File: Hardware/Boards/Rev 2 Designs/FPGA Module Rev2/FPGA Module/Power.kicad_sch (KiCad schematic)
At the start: 159 parts, among them U10 L78L33_SOT89, U11 INA236, U13 INA700AYWFR, U15 INA700AYWFR, U17 INA700AYWFR, U19 INA700AYWFR, U24 MP8796, U25 MP8796, U9 LT7200S

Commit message: Updates to FPGA and IO Module, layout studies and reference designs
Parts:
- removed C146, C147, C148, C161, C162, C163: 22uF, Capacitor_SMD:C_0805_2012Metric, symbol Device:C_Small
- removed C149, C164: 100nF, Capacitor_SMD:C_0201_0603Metric, symbol Device:C_Small
- removed C150, C165: 220nF, Capacitor_SMD:C_0201_0603Metric, symbol Device:C_Small
- removed C151: 1.8nF, Capacitor_SMD:C_0201_0603Metric, symbol Device:C_Small
- removed C152, C153, C154, C157: 100uF, Capacitor_SMD:C_0805_2012Metric, symbol Device:C_Small
- removed C155, C156: 560uF, Capacitor_Tantalum_SMD:CP_EIA-7343-31_Kemet-D, symbol Device:C_Polarized_Small_US
- removed C158, C159, C167, C168: 4.7uF, Capacitor_SMD:C_0201_0603Metric, symbol Device:C_Small
- removed C160: 470nF, Capacitor_SMD:C_0201_0603Metric, symbol Device:C_Small
- removed D7: 0V85 PG, LED_SMD:LED_0603_1608Metric, symbol Device:LED
- removed L1, L4: 220nH, FPGA Module:IND_SRP6530A_BRN, symbol Device:L
- removed R133: 12K, Resistor_SMD:R_0201_0603Metric, symbol Device:R_US
- removed R134: 27K, Resistor_SMD:R_0201_0603Metric, symbol Device:R_US
- removed R135, R136, R149, R152, R153, R161: 0R, Resistor_SMD:R_0201_0603Metric, symbol Device:R_US
- removed R137, R156: 2.2R, Resistor_SMD:R_0603_1608Metric, symbol Device:R_US
- removed R138, R142, R57, R6, R7: 3.3K, Resistor_SMD:R_0201_0603Metric, symbol Device:R_US
- removed R143, R144: 10K, Resistor_SMD:R_0201_0603Metric, symbol Device:R_US
- removed R147, R167: 24K, Resistor_SMD:R_0201_0603Metric, symbol Device:R_US
- removed R148, R168: 81K, Resistor_SMD:R_0201_0603Metric, symbol Device:R_US
- removed U24, U25: MP8796, FPGA Module:TQFN-4x5_MP8796B_MNP, symbol FPGA Module:MP8796GVT
- added C? (x2): 4.7uF, Capacitor_SMD:C_0201_0603Metric, symbol Device:C_Small
- added C? (x10): 22uF, Capacitor_SMD:C_0805_2012Metric, symbol Device:C_Small
- added C? (x4): 100uF, Capacitor_SMD:C_0805_2012Metric, symbol Device:C_Small
- added C?: 300pF, Capacitor_SMD:C_0201_0603Metric, symbol Device:C_Small
- added C? (x2): 560uF, Capacitor_Tantalum_SMD:CP_EIA-7343-31_Kemet-D, symbol Device:C_Polarized_Small_US
- added C?: 100nF, Capacitor_SMD:C_0201_0603Metric, symbol Device:C_Small
- added C?: 100nF, Capacitor_SMD:C_0402_1005Metric, symbol Device:C_Small
- added C? (x2): 1uF, Capacitor_SMD:C_0402_1005Metric, symbol Device:C_Small
- added D?: 0V85 PG, LED_SMD:LED_0603_1608Metric, symbol Device:LED
- added L?: 100nH, FPGA Module:IND_SRP6530A_BRN, symbol Device:L
- added R?: 10K, Resistor_SMD:R_0201_0603Metric, symbol Device:R_US
- added R?: 14K, Resistor_SMD:R_0201_0603Metric, symbol Device:R_US
- added R?: 24.9K, Resistor_SMD:R_0201_0603Metric, symbol Device:R_US
- added R?: 2.2R, Resistor_SMD:R_0603_1608Metric, symbol Device:R_US
- added R?: 24K, Resistor_SMD:R_0201_0603Metric, symbol Device:R_US
- added R?: 3.3K, Resistor_SMD:R_0201_0603Metric, symbol Device:R_US
- added R?: 3.48k, Resistor_SMD:R_0201_0603Metric, symbol Device:R_US
- added U?: TDA38840AUMA1, FPGA Module:PG-IQFN-36-2, symbol FPGA Module:TDA38840AUMA1
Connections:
- net 0V85_EN: now also U?.27 (EN)
- net 0V85_PG: now also D?.2 (A), R?.1, U?.2 (PGOOD)
- net 0V85_SNS: now also C?.1, C?.1, C?.1, C?.1, C?.1, C?.1, C?.1, C?.1, L?.2, R?.2
- net 3V3_AON: now also R?.2
- net GND: now also C?.2, C?.2, C?.2, C?.2, C?.2, C?.2, C?.2, C?.2, C?.2, C?.2, C?.2, C?.2, C?.2, C?.2, C?.2, C?.2, C?.2, C?.2, C?.2, C?.2, C?.2, D?.1 (K), R?.1, R?.1, R?.1, R?.1, U?.31 (VSENM), U?.32 (AGND), U?.7 (PGND)
- net PP_VUSB: now also C?.1, C?.1, C?.1, C?.1, C?.1, C?.1, C?.1, C?.1, C?.1, C?.1, C?.1, C?.1, U?.20 (PVIN), U?.3 (VIN)
- new net: C?.1, C?.1, U?.4 (VCC/LDO), U?.5 (VDRV)
- new net: C?.2, R?.1, R?.2, U?.30 (FB)
- new net: R?.2, U?.36 (TON/MODE)
- new net: R?.2, U?.1 (ILIM)
- new net: C?.1, R?.1
- new net: R?.2, U?.26 (BOOT)
- new net: L?.1, U?.11 (SW)
- new net: C?.2, U?.25 (PHASE)
- new net: R?.2, U?.29 (SS/LATCH)
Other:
- moved on the sheet: C102, C110, C118, C140, C141, C142, C143, C144, C145, C166, C169, C170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

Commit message: FPGA Module Rev 2 Layout Begun
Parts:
- removed C172, C173: 47uF, Capacitor_SMD:C_0603_1608Metric, symbol Device:C_Small
- removed L7: 300nH, Inductor_SMD:L_Taiyo-Yuden_MD-3030, symbol Device:L
- removed R101: 3.3K, Resistor_SMD:R_0201_0603Metric, symbol Device:R_US
- removed R68, R73: 33R, Resistor_SMD:R_0201_0603Metric, symbol Device:R_US
- removed TP33, TP45: Test Point, FPGA Module:Test Point 0.5mm No Silk, symbol Connector:TestPoint
- removed U13: INA700AYWFR, FPGA Module:INA700_AYWFR, symbol FPGA Module:INA700
- added C95, C96: 22uF, Capacitor_SMD:C_0805_2012Metric, symbol Device:C_Small
- added C98: 100pF, Capacitor_SMD:C_0603_1608Metric, symbol Device:C_Small
- added L5: 1uH, Inductor_SMD:L_1210_3225Metric, symbol Device:L
- added M1: Fan_4pin, Connector:FanPinHeader_1x04_P2.54mm_Vertical, symbol Motor:Fan_4pin
- added R69: 33R, Resistor_SMD:R_0201_0603Metric, symbol Device:R_US
- added R75: 3.3K, Resistor_SMD:R_0201_0603Metric, symbol Device:R_US
- added TP26: Test Point, FPGA Module:Test Point 0.5mm No Silk, symbol Connector:TestPoint
- C94: value 100nF -> 22uF; footprint Capacitor_SMD:C_0201_0603Metric -> Capacitor_SMD:C_0805_2012Metric
- R57: renamed from R63; value 33K -> 43K
- R67: renamed from R141; value 8.06K -> 100K
- R70: value 3.3K -> 10K
- gave numbers to parts that had none: 33
- renumbered C175 to C100, C176 to C101, C177 to C102, C178 to C103, C180 to C104, C182 to C105, C184 to C106, C179 to C107, C181 to C108, C183 to C109, C185 to C110, C86 to C64, C73 to C65, C88 to C66, C89 to C67, C90 to C68, C118 to C69, C83 to C70, C84 to C71, C81 to C72, C82 to C73, C79 to C74, C80 to C75, C77 to C76, C78 to C77, C85 to C78, C144 to C79, C145 to C80, C140 to C81, C166 to C82, C169 to C83, C110 to C84, C92 to C85, C87 to C86, C141 to C87, C170 to C88, C171 to C89, C186 to C90, C142 to C92, C102 to C93, C143 to C97, C174 to C99, D8 to D10, D11 to D7, D10 to D8, L3 to L2, L5 to L3, L2 to L4, R56 to R35, R58 to R37, R61 to R39, R62 to R40, R96 to R45, R105 to R46, R106 to R47, R64 to R48, R65 to R49, R87 to R50, R91 to R51, R92 to R52, R66 to R53, R132 to R54, R146 to R55, R150 to R56, R139 to R58, R78 to R59, R94 to R60, R85 to R61, R76 to R62, R67 to R63, R140 to R64, R82 to R65, R83 to R66, R145 to R68, R151 to R71, R154 to R72, R155 to R73, R157 to R74, R98 to R76, R99 to R77, R100 to R78, R102 to R79, TP28 to TP22, TP47 to TP23, TP39 to TP24, TP36 to TP25, TP42 to TP27, TP43 to TP28, TP44 to TP29, TP46 to TP30, U15 to U11, U11 to U6, U19 to U7, U9 to U8, U17 to U9
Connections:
- net 0V9_ISNS_ALERT is gone; now on net GND: R70.1
- net +3V3: no longer C94.1, R70.2
- net GND: now also C95.2, C96.2, C98.2, M1.1 (-), R75.1
- net 0V85_FB: now reaches C63.2, R38.1, R41.2, U5.30 (FB)
- net 0V85_LX: now reaches L1.1, U5.11 (SW)
- net +0V9 renamed 5V0
- net 5V0: now also C94.1, C95.1, C96.1, L5.2, M1.2 (+)
- net 0V9_EN renamed 5V0_EN
- net 5V0_EN: now also R75.2, TP26.1
- net 0V9_FB renamed 5V0_FB
- net 0V9_LX renamed 5V0_LX
- net 5V0_LX: now also L5.1
- new net: C98.1, M1.4 (PWM), R69.1, R70.2
- new net FAN_PWM: R69.2
- no-connect marks 1 -> 4
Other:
- note added: "5V 1A"
- note removed: "0V9 3A"
- moved on the sheet: D6, L1, R36, R76, R77, R78, R79, TP27, TP28, TP29, TP30

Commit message: Completed B2B and HyperRam routing
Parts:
- M1: footprint Connector:FanPinHeader_1x04_P2.54mm_Vertical -> Connector_JST:JST_GH_SM04B-GHS-TB_1x04-1MP_P1.25mm_Horizontal
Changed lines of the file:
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@@
 			)
 		)
-		(property "Footprint" "Connector:FanPinHeader_1x04_P2.54mm_Vertical"
+		(property "Footprint" "Connector_JST:JST_GH_SM04B-GHS-TB_1x04-1MP_P1.25mm_Horizontal"
 			(at 360.68 315.976 0)
 			(effects

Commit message: Rev 2 PCB's and Heatsink PCB's complete
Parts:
- removed C78: 1uF, Capacitor_SMD:C_0402_1005Metric, symbol Device:C_Small
- C98: footprint Capacitor_SMD:C_0603_1608Metric -> Capacitor_SMD:C_0201_0603Metric
- M1: footprint Connector_JST:JST_GH_SM04B-GHS-TB_1x04-1MP_P1.25mm_Horizontal -> Connector_JST:JST_SH_BM04B-SRSS-TB_1x04-1MP_P1.00mm_Vertical
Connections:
- net +0V85: now also C62.1, C63.1, R38.2
- net 0V85_SNS: no longer C62.1, C63.1, R38.2
- net FAN_PWM: now also R70.2
- net at C98.1, M1.4 (PWM), R69.1: no longer R70.2
- net 0V9_PG renamed 5V0_PG
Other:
- moved on the sheet: C62, R70

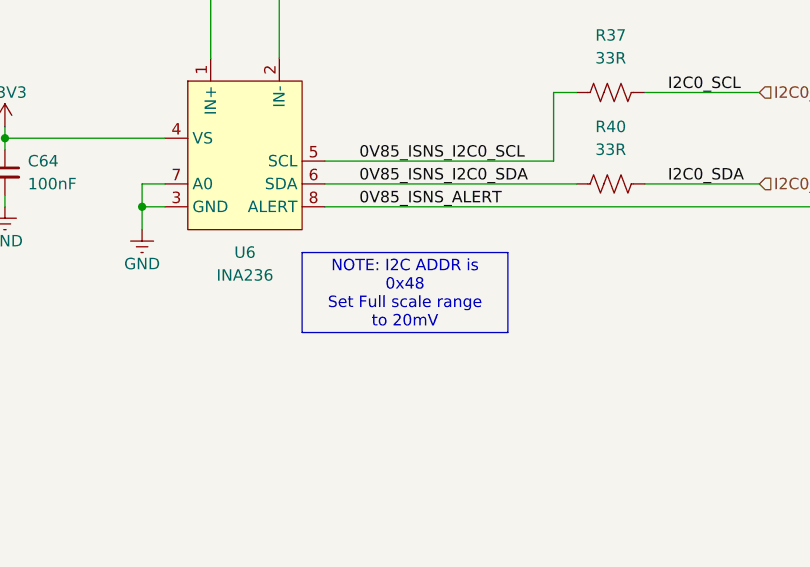
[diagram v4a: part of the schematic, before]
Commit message: Updated Schematics & created pixel combiner HDL
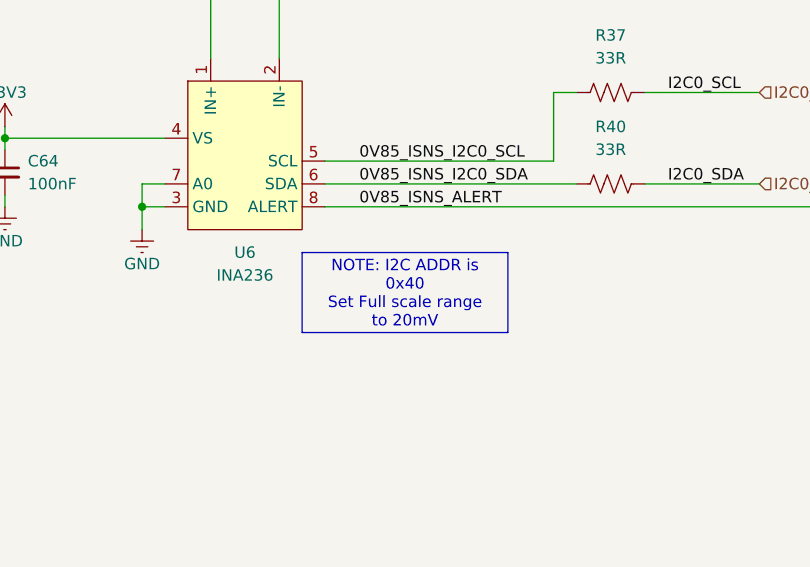
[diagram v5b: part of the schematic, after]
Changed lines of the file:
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@@
 		(rev "2.0")
 		(company "Drexel University")
-		(comment 1 "Designed by Michael Haahr")
+		(comment 1 "Designed by John Hofmeyr")
 	)
 	(junction
@@
 		)
 	)
-	(text_box "NOTE: I2C ADDR is 0x48\nSet Full scale range to 20mV"
+	(text_box "NOTE: I2C ADDR is 0x40\nSet Full scale range to 20mV"
 		(exclude_from_sim no)
 		(at 406.4 111.76 0)

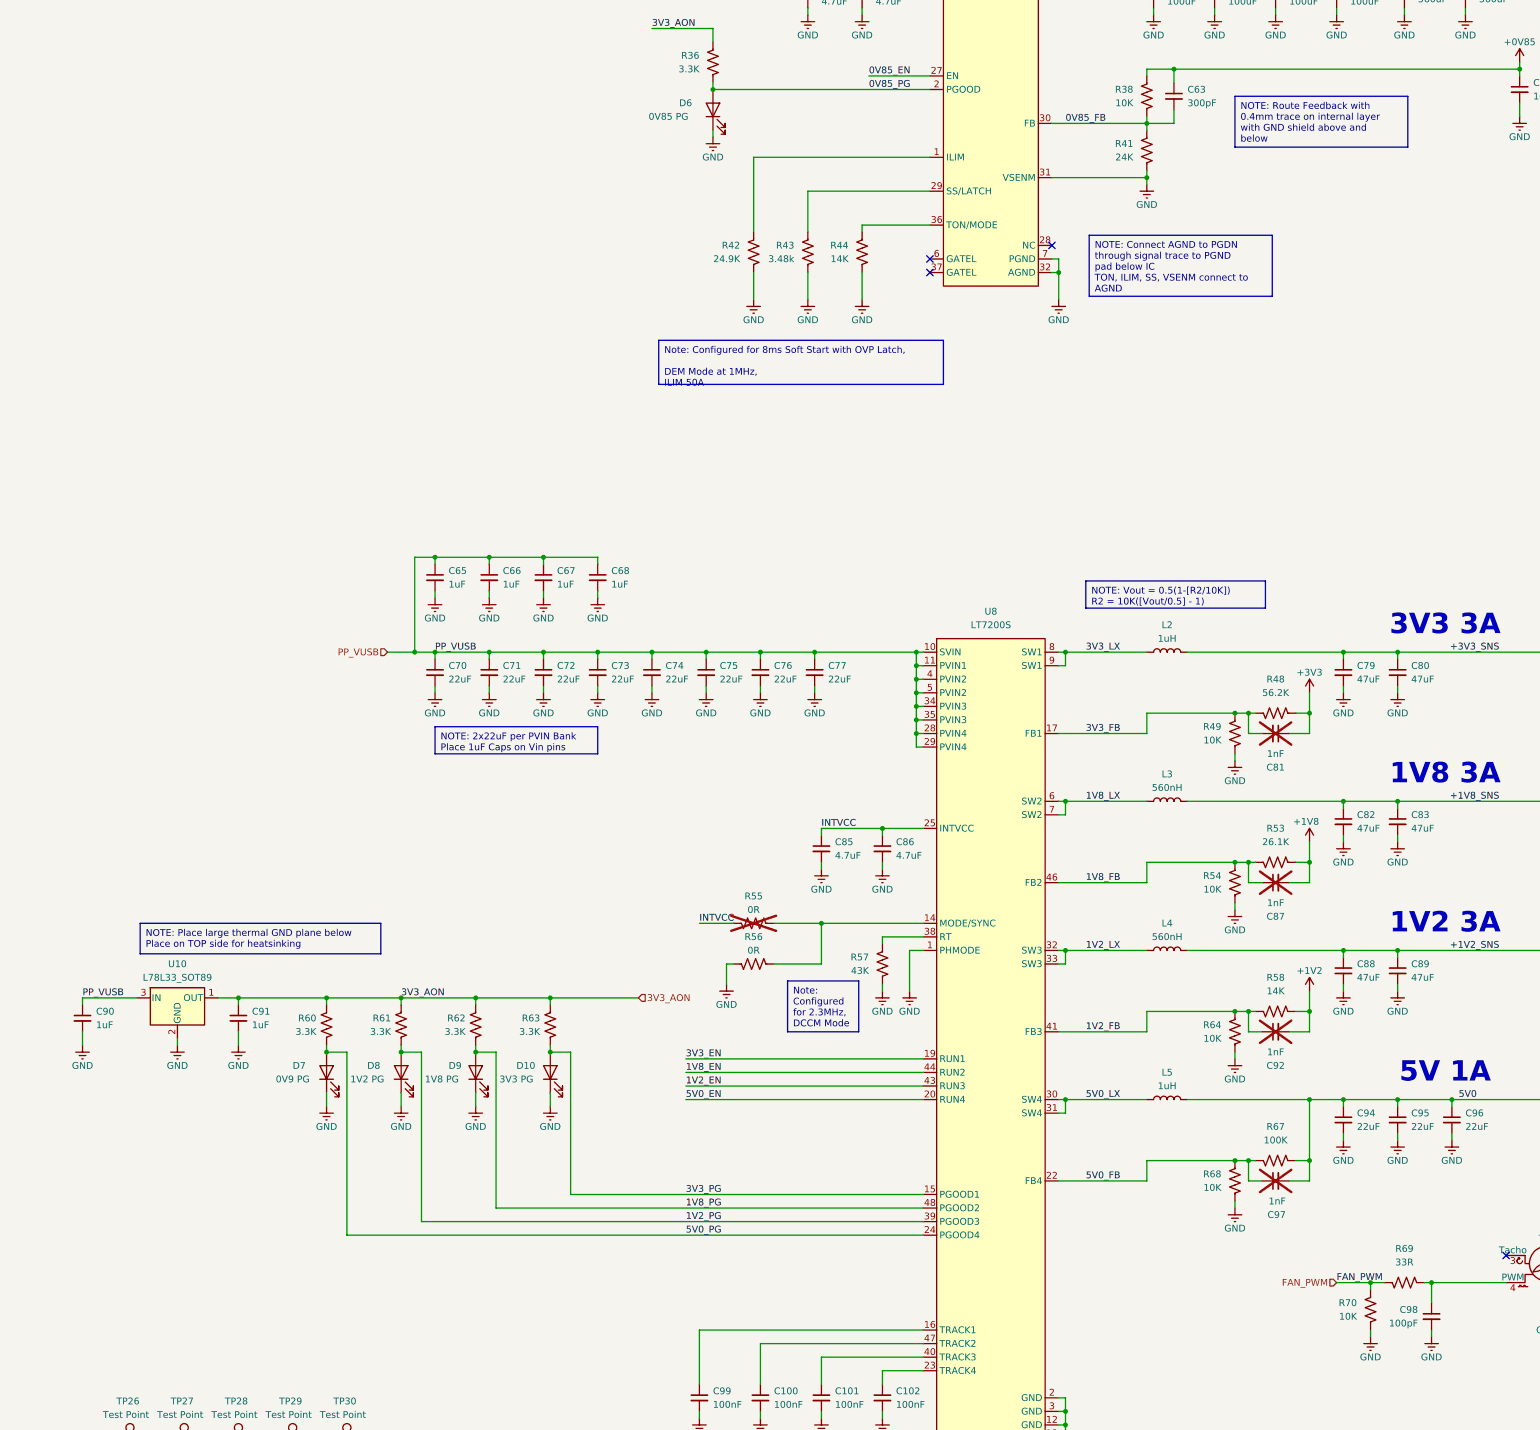
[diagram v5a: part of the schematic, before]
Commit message: Minor FPGA Bom updates
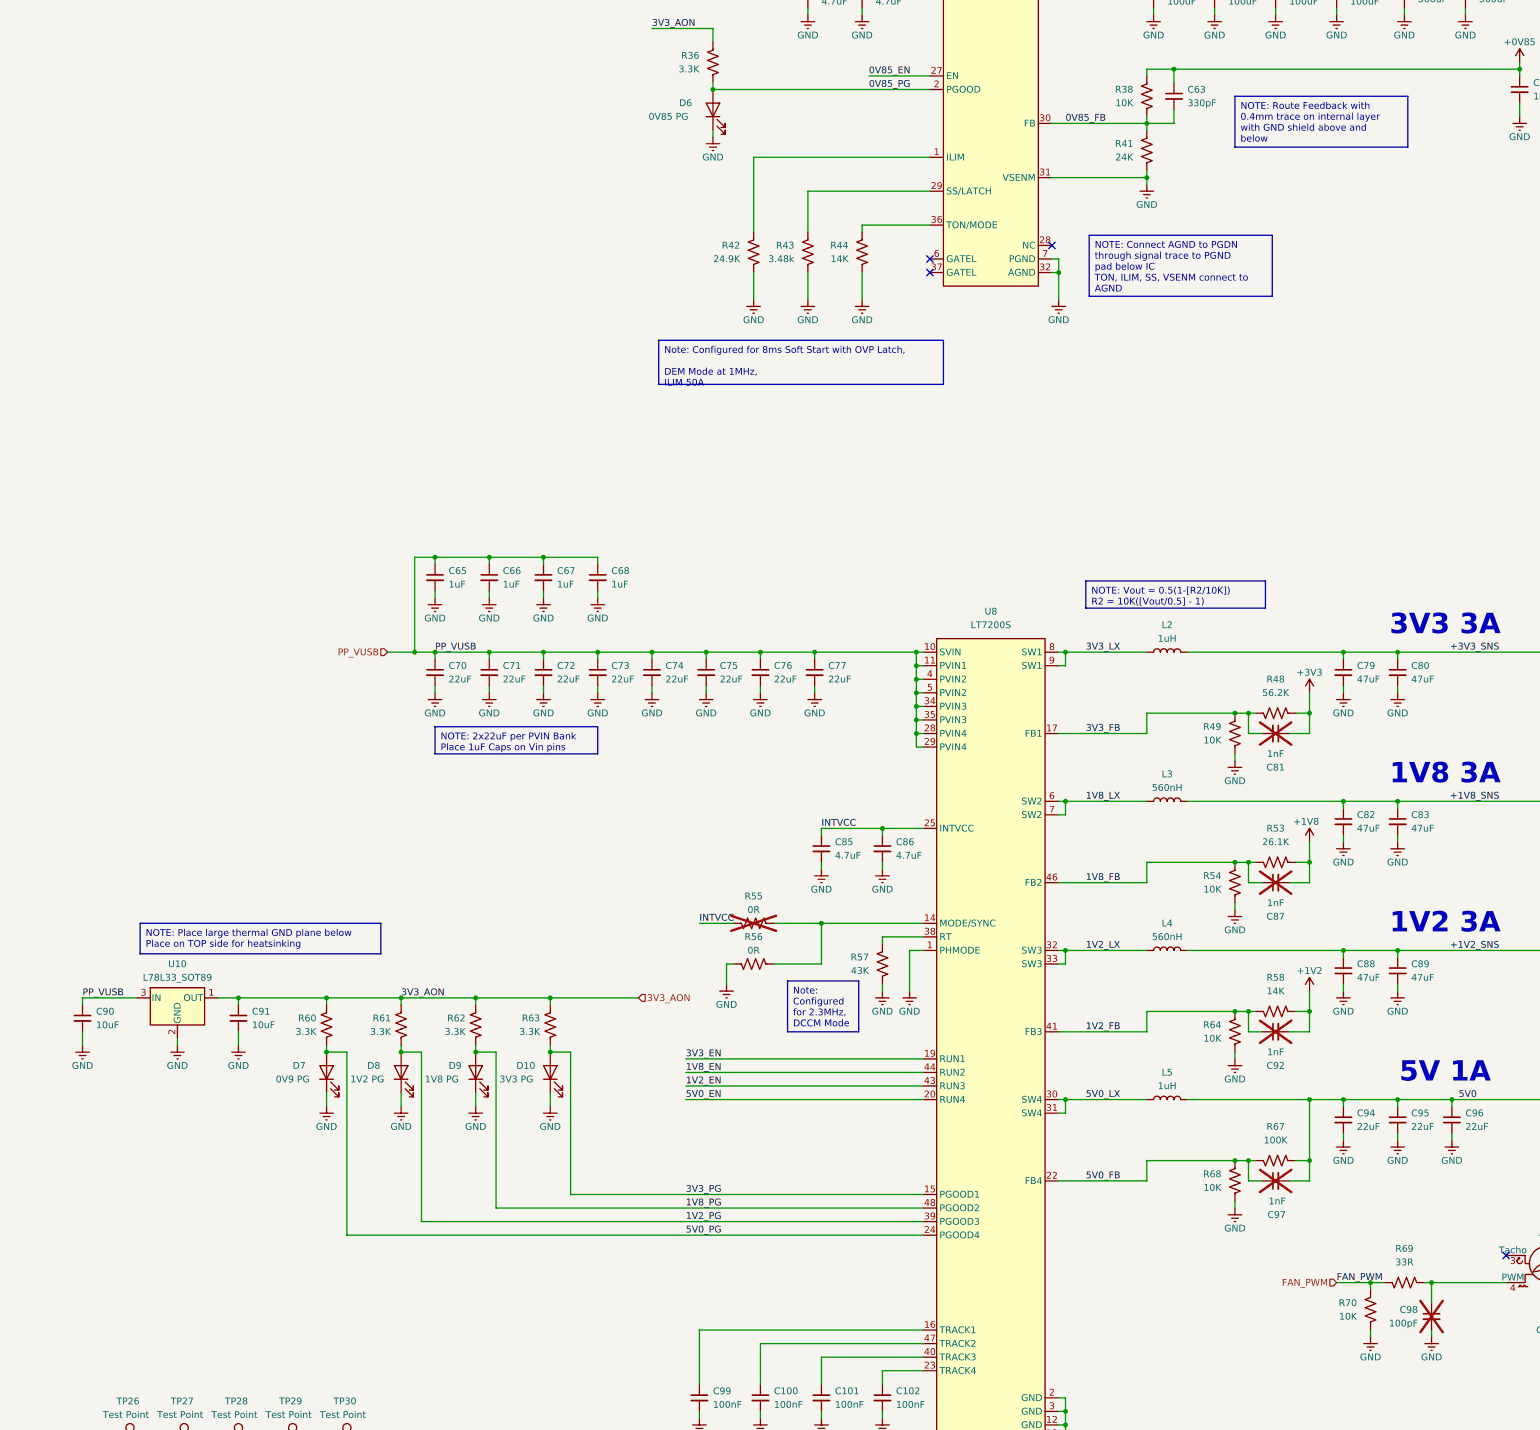
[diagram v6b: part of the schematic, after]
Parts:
- C63: value 300pF -> 330pF
- C90, C91: value 1uF -> 10uF
- C98: now not fitted
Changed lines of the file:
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@@
 			)
 		)
-		(property "Value" "1uF"
+		(property "Value" "10uF"
 			(at 118.11 270.5162 0)
 			(effects
@@
 			)
 		)
-		(property "Value" "300pF"
+		(property "Value" "330pF"
 			(at 293.37 97.7962 0)
 			(effects
@@
 		(in_bom yes)
 		(on_board yes)
-		(dnp no)
+		(dnp yes)
 		(fields_autoplaced yes)
 		(property "Reference" "C98"
@@
 			)
 		)
-		(property "Value" "1uF"
+		(property "Value" "10uF"
 			(at 88.9 270.5162 0)
 			(effects

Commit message: Updated main to match john-dev
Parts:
- R70: now not fitted
